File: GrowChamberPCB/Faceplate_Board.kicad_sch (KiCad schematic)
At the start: 4 parts, among them J10 Conn_01x24_Pin, J6 Conn_01x04_Pin

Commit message: Working on faceplate
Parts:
- removed J6: Conn_01x04_Pin, symbol Connector:Conn_01x04_Pin
- removed JP4: 5V UART Power, symbol Jumper:Jumper_2_Small_Open
- removed JP5: 3.3V UART Power, symbol Jumper:Jumper_2_Small_Open
- added J12: Fogger Fill Solenoid, symbol Connector:Conn_01x02_Pin
- added J13: Drain Solenoid, symbol Connector:Conn_01x02_Pin
- added J14: Glycol Solenoid, symbol Connector:Conn_01x02_Pin
- added J15: Fogger Disc, symbol Connector:Conn_01x02_Pin
- added J16: Fogger Float, symbol Connector:Conn_01x02_Pin
- added J17: Drain Level, symbol Connector:Conn_01x02_Pin
- added J18: Radiator Fans Con, symbol Connector:Conn_01x02_Pin
- added J19: Soil Moisture 2, Connector_Molex:Molex_KK-254_AE-6410-03A_1x03_P2.54mm_Vertical, symbol Connector:Conn_01x03_Pin
- added J20: Soil Moisture 3, Connector_Molex:Molex_KK-254_AE-6410-03A_1x03_P2.54mm_Vertical, symbol Connector:Conn_01x03_Pin
- added J21: Soil Moisture 1, Connector_Molex:Molex_KK-254_AE-6410-03A_1x03_P2.54mm_Vertical, symbol Connector:Conn_01x03_Pin
- added J22: Fan Connector, symbol Connector:Conn_01x04_Pin
- added J23: SCD30 Connector, symbol Connector:Conn_01x04_Pin
- added J25: Screw_Terminal_01x02, symbol Connector:Screw_Terminal_01x02
- added J6: UART, Connector_Molex:Molex_KK-254_AE-6410-03A_1x03_P2.54mm_Vertical, symbol Connector:Conn_01x03_Pin
- added J9: Water Solenoid, symbol Connector:Conn_01x02_Pin
- added SW3: BootSwitch, symbol Switch:SW_Push
- added SW4: ResetButton, symbol Switch:SW_Push
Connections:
- net 12V_FP: now also J22.2 (Pin_2)
- net 3.3V_FP: now also J23.1 (Pin_1)
- net 5V_FP: now also J19.2 (Pin_2), J20.2 (Pin_2), J21.2 (Pin_2)
- net DrainSol_FP: now also J13.1 (Pin_1)
- net Drain_Level_FP: now also J17.1 (Pin_1)
- net External_Fan_PWM_FP: now also J22.4 (Pin_4)
- net FoggerSol_FP: now also J12.1 (Pin_1)
- net Fogger_Basin_Float_Switch_FP: now also J16.1 (Pin_1)
- net GPIO1_FP: now also J21.1 (Pin_1)
- net GPIO2_FP: now also J19.1 (Pin_1)
- net GPIO4_FP: now also J20.1 (Pin_1)
- net GlycolSol_FP: now also J14.1 (Pin_1)
- net Gnd_FP: now also J12.2 (Pin_2), J13.2 (Pin_2), J14.2 (Pin_2), J16.2 (Pin_2), J17.2 (Pin_2), J18.2 (Pin_2), J19.3 (Pin_3), J20.3 (Pin_3), J21.3 (Pin_3), J22.1 (Pin_1), J23.2 (Pin_2), J6.1 (Pin_1), J9.2 (Pin_2), SW3.2, SW4.2
- net Piezo1_FP: now also J15.2 (Pin_2)
- net Piezo2_FP: now also J15.1 (Pin_1)
- net RXD0_FP: now also J6.2 (Pin_2)
- net RadiatorFans_FP: now also J18.1 (Pin_1)
- net SCL_FP: now also J23.3 (Pin_3)
- net SDA_FP: now also J23.4 (Pin_4)
- net TXD0_FP: now also J6.3 (Pin_3)
- net WaterSol_FP: now also J9.1 (Pin_1)
- net Fan_Tach_FP: now reaches J10.22 (Pin_22)
- net Reset_SW_FP: now reaches J10.23 (Pin_23)
- net Reset_SW_FP: now also SW4.1
- net BootMode_FP: now reaches J10.24 (Pin_24)
- net BootMode_FP: now also SW3.1
- new net 12V_LED_FP: J25.1 (Pin_1)
- new net Fan_Tach: J22.3 (Pin_3)
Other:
- note added: "LED connector - Separate screw terminal"
- note removed: "TX and RX swapped for Faceplate. Label external to match."
- moved on the sheet: J10

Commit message: final schematic
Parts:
- added J24: LED_Con, symbol Connector:Conn_01x02_Pin
- added J4, J5: Glycol Fans, symbol Connector:Conn_01x02_Pin
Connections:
- net Fan_Tach is gone; now on net Fan_Tach_FP: J22.3 (Pin_3)
- net 5V_FP: now also J23.1 (Pin_1)
- net GlycolSol_FP: now also J4.1 (Pin_1)
- net Gnd_FP: now also J25.2 (Pin_2), J24.2 (Pin_2), J4.2 (Pin_2), J5.2 (Pin_2)
- net 12V_LED_FP: no longer names the net of J25.1 (Pin_1)
- net 12V_LED_FP: now also J24.1 (Pin_1)
- net 3.3V_FP renamed Circ_Fan_FP
- net Circ_Fan_FP: now also J5.1 (Pin_1); no longer J23.1 (Pin_1)
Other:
- moved on the sheet: J12, J13, J14, J18, J23, J6, J9, SW3, SW4

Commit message: Assigning footprints and stuff
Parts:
- removed J10: Conn_01x24_Pin, symbol Connector:Conn_01x24_Pin
- added J11: Conn_01x26_Pin, symbol Connector:Conn_01x26_Pin
- J18: value Radiator Fans Con -> Heater Fans Con
- J5: value Glycol Fans -> Circ Fans
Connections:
- net 12V_FP: now also J11.4 (Pin_4)
- net 5V_FP: now also J11.5 (Pin_5)
- net BootMode_FP: now also J11.24 (Pin_24)
- net Circ_Fan_FP: now also J11.6 (Pin_6)
- net DrainSol_FP: now also J11.17 (Pin_17)
- net Drain_Level_FP: now also J11.20 (Pin_20)
- net External_Fan_PWM_FP: now also J11.21 (Pin_21)
- net Fan_Tach_FP: now also J11.22 (Pin_22)
- net FoggerSol_FP: now also J11.18 (Pin_18)
- net Fogger_Basin_Float_Switch_FP: now also J11.1 (Pin_1)
- net GPIO1_FP: now also J11.12 (Pin_12)
- net GPIO2_FP: now also J11.11 (Pin_11)
- net GPIO4_FP: now also J11.10 (Pin_10)
- net GlycolSol_FP: now also J11.15 (Pin_15); no longer J4.1 (Pin_1)
- net Piezo1_FP: now also J11.14 (Pin_14)
- net Piezo2_FP: now also J11.13 (Pin_13)
- net RXD0_FP: now also J11.3 (Pin_3)
- net Reset_SW_FP: now also J11.23 (Pin_23)
- net SCL_FP: now also J11.9 (Pin_9)
- net SDA_FP: now also J11.8 (Pin_8)
- net TXD0_FP: now also J11.2 (Pin_2)
- net WaterSol_FP: now also J11.16 (Pin_16)
- net RadiatorFans_FP renamed Heater Fans_FP
- net Heater Fans_FP: now also J11.19 (Pin_19)
- new net GlycolFans: J11.7 (Pin_7), J4.1 (Pin_1)
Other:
- moved on the sheet: J17, J5

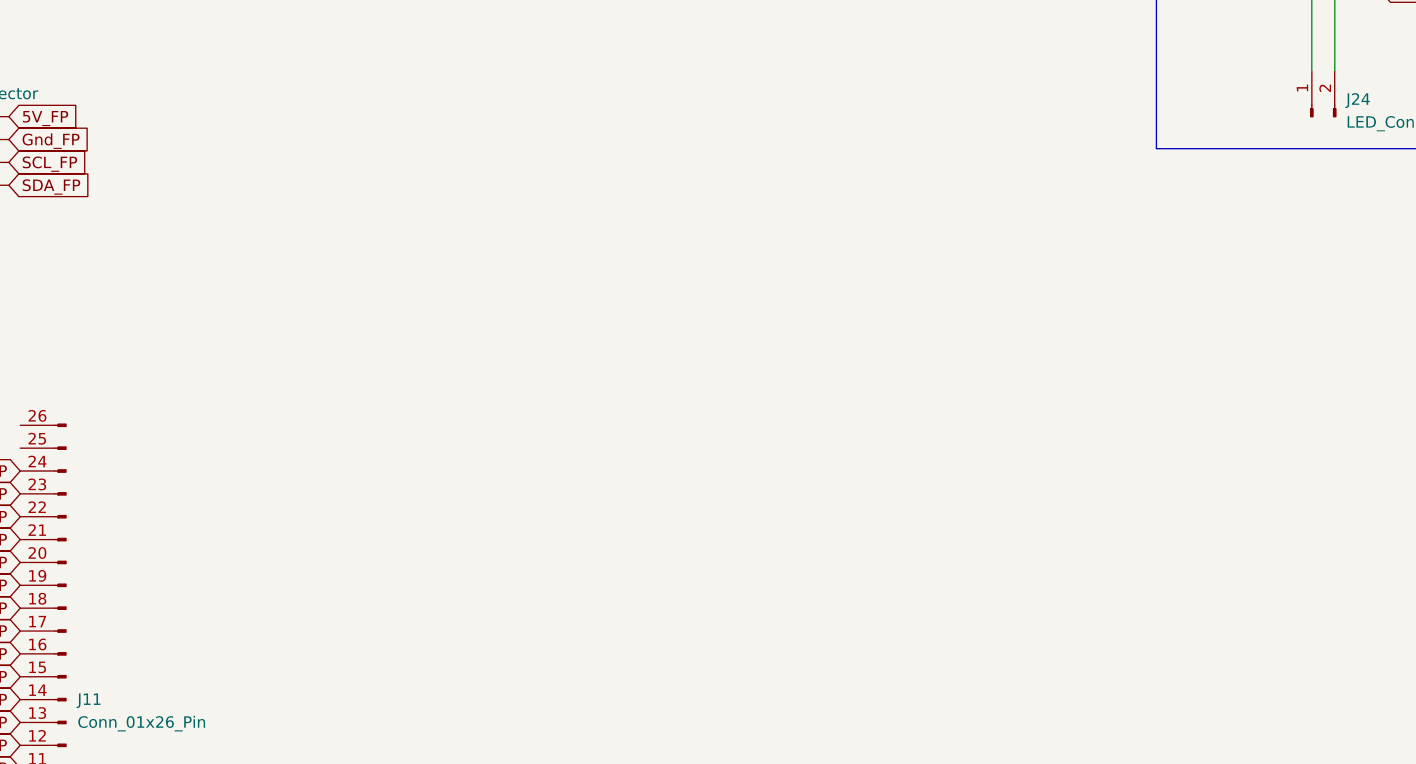
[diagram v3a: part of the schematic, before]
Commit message: added i2c led controller
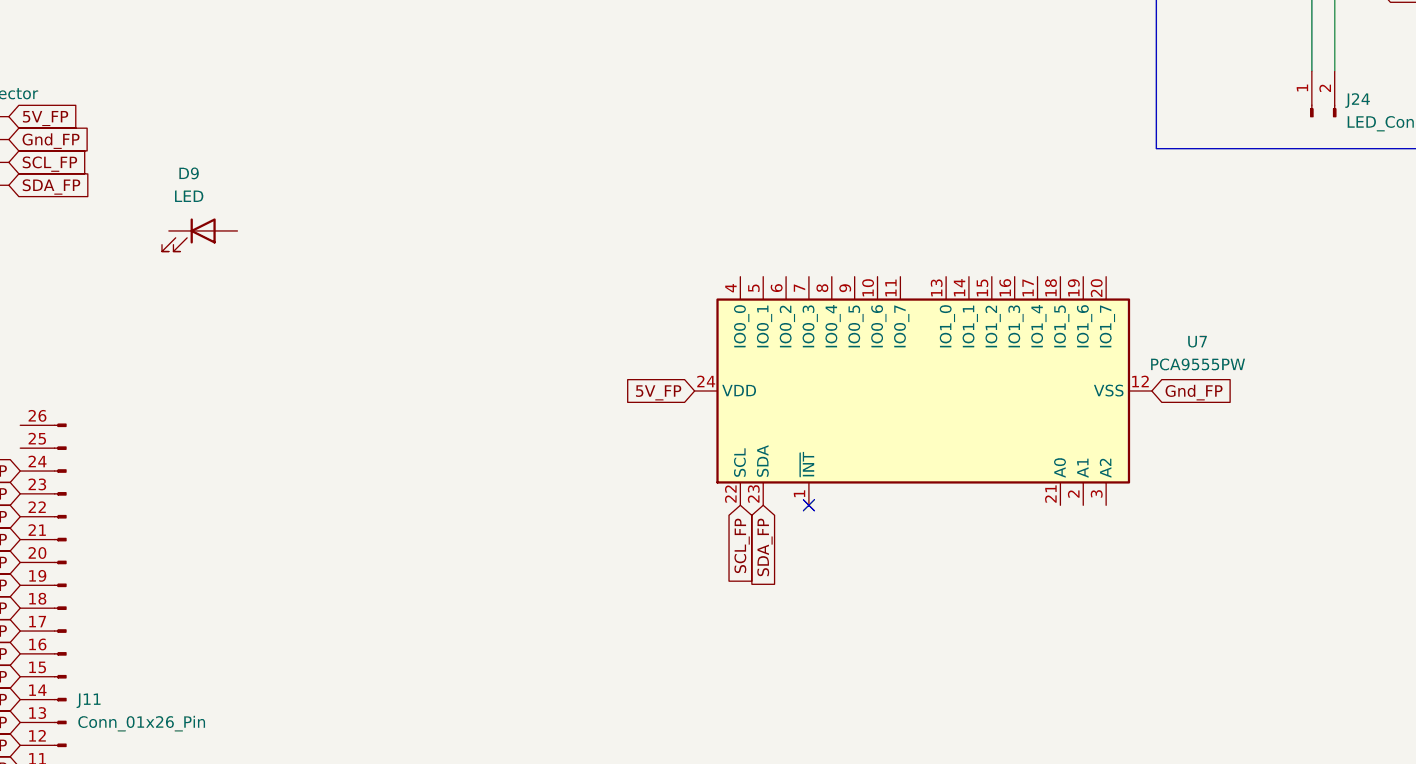
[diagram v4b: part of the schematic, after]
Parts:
- added D9: LED, symbol Device:LED
- added U7: PCA9555PW, Package_SO:TSSOP-24_4.4x7.8mm_P0.65mm, symbol Interface_Expansion:PCA9555PW
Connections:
- net 5V_FP: now also U7.24 (VDD)
- net Gnd_FP: now also U7.12 (VSS)
- net SCL_FP: now also U7.22 (SCL)
- net SDA_FP: now also U7.23 (SDA)
- no-connect marks 0 -> 1

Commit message: struggling to make BOM
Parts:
- removed J25: Screw_Terminal_01x02, symbol Connector:Screw_Terminal_01x02
- added D13: Glycol LED, symbol Device:LED
- added D15: Drain Solenoid LED, symbol Device:LED
- added D16: Fogger FIll Solenoid LED, symbol Device:LED
- added D17: Water Solenoid LED, symbol Device:LED
- added D18: Heater Fans LED, symbol Device:LED
- added D19: Circ Fans LED, symbol Device:LED
- added D20: Heater On LED, symbol Device:LED
- added D23: PowerOn_LED, symbol Device:LED
- added J8: Screw_Terminal_01x03, symbol Connector:Screw_Terminal_01x03
- added R34, R38, R40, R41, R42, R43, R44, R45, R48: 1000, symbol Device:R
- added R35, R50: 20k, symbol Device:R
- added R36, R49: 10k, symbol Device:R
- D9: value LED -> LED LED
- J19, J20, J21, J6: footprint Connector_Molex:Molex_KK-254_AE-6410-03A_1x03_P2.54mm_Vertical -> (none)
- J24: value LED_Con -> Conn_01x02_Pin
- U7: footprint Package_SO:TSSOP-24_4.4x7.8mm_P0.65mm -> (none)
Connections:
- net 12V_FP: now also D9.2 (A), J12.2 (Pin_2), J13.2 (Pin_2), J14.2 (Pin_2), J18.2 (Pin_2), J4.2 (Pin_2), J5.2 (Pin_2), J9.2 (Pin_2), D13.2 (A), D15.2 (A), D16.2 (A), D17.2 (A), D18.2 (A), D19.2 (A), D20.2 (A), D23.2 (A); no longer J11.4 (Pin_4)
- net 5V_FP: now also J11.4 (Pin_4), R36.1, R49.1; no longer J11.5 (Pin_5)
- net BootMode_FP: now also J11.22 (Pin_22); no longer J11.24 (Pin_24)
- net Circ_Fan_FP: now also J11.5 (Pin_5), R44.1; no longer J11.6 (Pin_6)
- net DrainSol_FP: now also J11.15 (Pin_15), R40.1; no longer J11.17 (Pin_17)
- net Drain_Level_FP: now also J11.18 (Pin_18); no longer J11.20 (Pin_20)
- net External_Fan_PWM_FP: now also J11.19 (Pin_19); no longer J11.21 (Pin_21)
- net Fan_Tach_FP: now also J11.20 (Pin_20); no longer J11.22 (Pin_22)
- net FoggerSol_FP: now also J11.16 (Pin_16), R41.1; no longer J11.18 (Pin_18)
- net GPIO1_FP: now also J11.10 (Pin_10); no longer J11.12 (Pin_12)
- net GPIO2_FP: now also J11.9 (Pin_9); no longer J11.11 (Pin_11)
- net GPIO4_FP: now also J11.8 (Pin_8); no longer J11.10 (Pin_10)
- net GlycolSol_FP: now also J11.13 (Pin_13), J4.1 (Pin_1), R38.1; no longer J11.15 (Pin_15)
- net Gnd_FP: now also U7.2 (A1), U7.21 (A0), U7.3 (A2), R35.2, R48.1, R50.2; no longer J12.2 (Pin_2), J13.2 (Pin_2), J14.2 (Pin_2), J16.2 (Pin_2), J17.2 (Pin_2), J18.2 (Pin_2), J24.2 (Pin_2), J4.2 (Pin_2), J5.2 (Pin_2), J9.2 (Pin_2)
- net Heater Fans_FP: now also J11.17 (Pin_17), R43.1; no longer J11.19 (Pin_19)
- net Piezo1_FP: now also J11.12 (Pin_12); no longer J11.14 (Pin_14)
- net Piezo2_FP: now also J11.11 (Pin_11); no longer J11.13 (Pin_13)
- net Reset_SW_FP: now also J11.21 (Pin_21); no longer J11.23 (Pin_23)
- net SCL_FP: now also J11.7 (Pin_7); no longer J11.9 (Pin_9)
- net SDA_FP: now also J11.6 (Pin_6); no longer J11.8 (Pin_8)
- net WaterSol_FP: now also J11.14 (Pin_14), R42.1; no longer J11.16 (Pin_16)
- net FAE_LED: now reaches U7.4 (IO0_0)
- net HeaterFault_LED: now reaches U7.5 (IO0_1)
- net Fogger_LED: now reaches U7.6 (IO0_2)
- net WifiCom_LED: now reaches U7.7 (IO0_3)
- net ESPNow_LED: now reaches U7.8 (IO0_4)
- net Heartbeat_LED: now reaches U7.9 (IO0_5)
- net LEDs_FP: now reaches J24.1 (Pin_1)
- net LEDs_FP: now also J8.1 (Pin_1), R34.1
- net at D9.1 (K): now also R34.2
- removed net GlycolFans: J11.7 (Pin_7), J4.1 (Pin_1)
- new net: J17.2 (Pin_2), R49.2, R50.1
- new net: D17.1 (K), R42.2
- new net: D16.1 (K), R41.2
- new net: D19.1 (K), R44.2
- new net: J16.2 (Pin_2), R35.1, R36.2
- new net: D13.1 (K), R38.2
- new net: D23.1 (K), R48.2
- new net: D20.1 (K), R45.2
- new net: D18.1 (K), R43.2
- new net: D15.1 (K), R40.2
- new net 12V: J24.2 (Pin_2), J8.3 (Pin_3)
- new net Gnd: J8.2 (Pin_2)
- new net Heater_On_FP: J11.23 (Pin_23), R45.1
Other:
- note added: "5V to 3.3V Voltage Divider for Water Level Sensors"
- note added: "LED Connector and Screw Terminal"
- note removed: "LED connector - Separate screw terminal"
- moved on the sheet: J11, J12, J13, J14, J15, J16, J17, J18, J19, J20, J21, J22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

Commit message: BOM and footprints
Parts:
- added D10, D11, D12, D14: Water Solenoid LED, LED_THT:LED_D5.0mm, symbol Device:LED
- added D21: Fogger_LED, LED_THT:LED_D5.0mm, symbol Device:LED
- added D22: ESPNow_LED, LED_THT:LED_D5.0mm, symbol Device:LED
- added R12, R37, R39, R46, R47, R51: 1000, digikey-footprints:0805, symbol Device:R
- D13: value Glycol LED -> Water Solenoid LED; Manufacturer (none) -> Kingbright; Package (none) -> through-hole
- D15: value Drain Solenoid LED -> Water Solenoid LED; Manufacturer (none) -> Kingbright; Package (none) -> through-hole
- D16: value Fogger FIll Solenoid LED -> Water Solenoid LED; Manufacturer (none) -> Kingbright; Package (none) -> through-hole
- D17: Manufacturer (none) -> Kingbright; Package (none) -> through-hole
- D18: value Heater Fans LED -> FAE_LED; Manufacturer (none) -> Kingbright; Package (none) -> through-hole
- D19: value Circ Fans LED -> HeaterFault_LED; Manufacturer (none) -> Kingbright; Package (none) -> through-hole
- D20: value Heater On LED -> WifiCom_LED; Manufacturer (none) -> Kingbright; Package (none) -> through-hole
- D23: value PowerOn_LED -> Heartbeat_LED; Manufacturer (none) -> Kingbright; Package (none) -> through-hole
- D9: value LED LED -> Water Solenoid LED; Manufacturer (none) -> Kingbright; Package (none) -> through-hole
- J11: footprint (none) -> Connector_PinHeader_2.54mm:PinHeader_2x13_P2.54mm_Vertical
- J12: footprint (none) -> Connector_Molex:Molex_KK-254_AE-6410-05A_1x05_P2.54mm_Vertical
- J13, J14, J17, J18, J19, J20, J21, J22, J6, J8, J9: footprint (none) -> Connector_Molex:Molex_KK-254_AE-6410-03A_1x03_P2.54mm_Vertical
- J15, J16, J24, J4, J5: footprint (none) -> Connector_Molex:Molex_KK-254_AE-6410-02A_1x02_P2.54mm_Vertical
- J23: footprint (none) -> Connector_Molex:Molex_KK-254_AE-6410-04A_1x04_P2.54mm_Vertical
- R34, R35, R36, R38, R40, R41, R42, R43, R44, R45, R48, R49, R50: footprint (none) -> digikey-footprints:0805
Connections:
- net 12V_FP: now also D10.2 (A), D11.2 (A), D12.2 (A), D14.2 (A), R12.1, R37.1, R39.1, R46.1, R47.1, R51.1; no longer D18.2 (A), D19.2 (A), D20.2 (A), D23.2 (A)
- net ESPNow_LED: now also D22.1 (K)
- net FAE_LED: now also D18.1 (K)
- net Fogger_LED: now also D21.1 (K)
- net Heartbeat_LED: now also D23.1 (K)
- net HeaterFault_LED: now also D19.1 (K)
- net WifiCom_LED: now also D20.1 (K)
- net at D16.1 (K): now also R48.2; no longer R41.2
- net at R44.2: now also D13.1 (K); no longer D19.1 (K)
- net at D9.1 (K): now also R41.2; no longer R34.2
- net at R38.2: now also D11.1 (K); no longer D13.1 (K)
- net at R45.2: now also D14.1 (K); no longer D20.1 (K)
- net at R43.2: now also D12.1 (K); no longer D18.1 (K)
- net at R40.2: now also D10.1 (K); no longer D15.1 (K)
- new net: D19.2 (A), R37.2
- new net: D20.2 (A), R46.2
- new net: D18.2 (A), R12.2
- new net: D21.2 (A), R39.2
- new net: D22.2 (A), R47.2
- new net: D23.2 (A), R51.2
- new net: D15.1 (K), R34.2

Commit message: working on BOM and footprints
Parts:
- removed SW3: BootSwitch, symbol Switch:SW_Push
- removed SW4: ResetButton, symbol Switch:SW_Push
- added SW1: BootMode_Switch, symbol Switch:SW_SPDT
- added SW2: ResetButton_External, symbol Switch:SW_Push
- D10, D11, D12, D14: value Water Solenoid LED -> LED; MFG Part Number (none) -> WP7113ID
- D13, D15, D16, D17, D9: value Water Solenoid LED -> LED; footprint (none) -> LED_THT:LED_D5.0mm; MFG Part Number (none) -> WP7113ID
- D18: value FAE_LED -> LED; footprint (none) -> LED_THT:LED_D5.0mm; MFG Part Number (none) -> WP7113ID
- D19: value HeaterFault_LED -> LED; footprint (none) -> LED_THT:LED_D5.0mm; MFG Part Number (none) -> WP7113ID
- D20: value WifiCom_LED -> LED; footprint (none) -> LED_THT:LED_D5.0mm; MFG Part Number (none) -> WP7113ID
- D21: value Fogger_LED -> LED; MFG Part Number (none) -> WP7113ID
- D22: value ESPNow_LED -> LED; MFG Part Number (none) -> WP7113ID
- D23: value Heartbeat_LED -> LED; footprint (none) -> LED_THT:LED_D5.0mm; MFG Part Number (none) -> WP7113ID
- U7: value PCA9555PW -> PCA9555PW,118; footprint (none) -> digikey-footprints:TSSOP-24_W4.40mm; MFG Part Number (none) -> PCA9555PW,118; Manufacturer (none) -> NXP Semicon; Package (none) -> TSSOP-24; Type (SMD/thru-hole, etc.) (none) -> SMD
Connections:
- net BootMode_FP: now also SW1.1 (A)
- net Gnd_FP: now also SW1.2 (B), SW2.2
- net Reset_SW_FP renamed Reset_Button_FP
- net Reset_Button_FP: now also SW2.1
- no-connect marks 1 -> 2
